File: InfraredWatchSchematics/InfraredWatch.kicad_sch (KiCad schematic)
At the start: 45 parts, among them J1 USB_C_Receptacle_USB2.0_14P, J2 Conn_Coaxial, J3 Micro_SD_Card_Det2, P1 XC9265A331MR-G, SW1 SW_Push, U1 STM32WB55CGU6, U2 MCP73831-5-OT, U3 USBLC6-2SC6, Y1 32MHz, Y2 32.768kHz

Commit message: Sat Mar 28 22:20:19 EDT 2026
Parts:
- removed J1: USB_C_Receptacle_USB2.0_14P, symbol Connector:USB_C_Receptacle_USB2.0_14P
- removed J2: Conn_Coaxial, symbol Connector:Conn_Coaxial
- added AE1: Antenna_Loop, symbol Device:Antenna_Loop
- added C20, C21, C22: 100nF, Capacitor_SMD:C_0402_1005Metric_Pad0.74x0.62mm_HandSolder, symbol Device:C
- added J4: USB_C_Receptacle_USB2.0_16P, Connector_USB:USB_C_Receptacle_G-Switch_GT-USB-7010ASV, symbol Connector:USB_C_Receptacle_USB2.0_16P
- added R10, R11, R12: 100, Resistor_SMD:R_0201_0603Metric_Pad0.64x0.40mm_HandSolder, symbol Device:R
- added R6, R7, R8: 5.1k, Resistor_SMD:R_0603_1608Metric_Pad0.98x0.95mm_HandSolder, symbol Device:R
- added SW1, SW2, SW3: SW_Push, symbol Switch:SW_Push
- C1: renamed from C17; footprint (none) -> Capacitor_SMD:C_0603_1608Metric_Pad1.08x0.95mm_HandSolder
- C10: renamed from C9; footprint (none) -> Capacitor_SMD:C_0603_1608Metric_Pad1.08x0.95mm_HandSolder
- C11: renamed from C19; footprint (none) -> Capacitor_SMD:C_0201_0603Metric_Pad0.64x0.40mm_HandSolder
- C12: renamed from C10; footprint (none) -> Capacitor_SMD:C_0402_1005Metric_Pad0.74x0.62mm_HandSolder
- C13: renamed from C8; footprint (none) -> Capacitor_SMD:C_0402_1005Metric_Pad0.74x0.62mm_HandSolder
- C14: renamed from C20; footprint (none) -> Capacitor_SMD:C_0402_1005Metric_Pad0.74x0.62mm_HandSolder
- C15: renamed from C12; footprint (none) -> Capacitor_SMD:C_0402_1005Metric_Pad0.74x0.62mm_HandSolder
- C16: renamed from C13; footprint (none) -> Capacitor_SMD:C_0402_1005Metric_Pad0.74x0.62mm_HandSolder
- C17: renamed from C11; footprint (none) -> Capacitor_SMD:C_0603_1608Metric_Pad1.08x0.95mm_HandSolder
- C18: renamed from C14; footprint (none) -> Capacitor_SMD:C_0402_1005Metric_Pad0.74x0.62mm_HandSolder
- C19: renamed from C15; footprint (none) -> Capacitor_SMD:C_0402_1005Metric_Pad0.74x0.62mm_HandSolder
- C2: renamed from C7; footprint (none) -> Capacitor_SMD:C_0603_1608Metric_Pad1.08x0.95mm_HandSolder
- C23: renamed from C16; footprint (none) -> Capacitor_SMD:C_0402_1005Metric_Pad0.74x0.62mm_HandSolder
- C3: renamed from C6; footprint (none) -> Capacitor_SMD:C_0402_1005Metric_Pad0.74x0.62mm_HandSolder
- C4: renamed from C5; footprint (none) -> Capacitor_SMD:C_0402_1005Metric_Pad0.74x0.62mm_HandSolder
- C5: renamed from C4; footprint (none) -> Capacitor_SMD:C_0402_1005Metric_Pad0.74x0.62mm_HandSolder
- C6: renamed from C18; footprint (none) -> Capacitor_SMD:C_0201_0603Metric_Pad0.64x0.40mm_HandSolder
- C7: renamed from C3; footprint (none) -> Capacitor_SMD:C_0402_1005Metric_Pad0.74x0.62mm_HandSolder
- C8: renamed from C2; footprint (none) -> Capacitor_SMD:C_0402_1005Metric_Pad0.74x0.62mm_HandSolder
- C9: renamed from C1; footprint (none) -> Capacitor_SMD:C_0402_1005Metric_Pad0.74x0.62mm_HandSolder
- D1: renamed from D2; footprint (none) -> LED_SMD:LED_0402_1005Metric_Pad0.77x0.64mm_HandSolder
- D2: renamed from D1; footprint (none) -> LED_SMD:LED_0402_1005Metric_Pad0.77x0.64mm_HandSolder
- L1: renamed from L4; footprint (none) -> Inductor_SMD:L_0603_1608Metric_Pad1.05x0.95mm_HandSolder
- L2: renamed from L1; footprint (none) -> Inductor_SMD:L_0603_1608Metric_Pad1.05x0.95mm_HandSolder
- L3: renamed from L2; footprint (none) -> Inductor_SMD:L_0603_1608Metric_Pad1.05x0.95mm_HandSolder
- L4: renamed from L3; footprint (none) -> Inductor_SMD:L_0603_1608Metric_Pad1.05x0.95mm_HandSolder
- R1: renamed from R7; footprint (none) -> Resistor_SMD:R_0603_1608Metric_Pad0.98x0.95mm_HandSolder
- R13: renamed from R4; footprint (none) -> Resistor_SMD:R_0201_0603Metric_Pad0.64x0.40mm_HandSolder
- R2: renamed from R6; footprint (none) -> Resistor_SMD:R_0201_0603Metric_Pad0.64x0.40mm_HandSolder
- R3: renamed from R1; footprint (none) -> Resistor_SMD:R_0603_1608Metric_Pad0.98x0.95mm_HandSolder
- R4: renamed from R2; footprint (none) -> Resistor_SMD:R_0603_1608Metric_Pad0.98x0.95mm_HandSolder
- R5: footprint (none) -> Resistor_SMD:R_0603_1608Metric_Pad0.98x0.95mm_HandSolder
- R9: renamed from R3; footprint (none) -> Resistor_SMD:R_0603_1608Metric_Pad0.98x0.95mm_HandSolder
- Y1: renamed from Y2; footprint (none) -> Crystal:Crystal_SMD_2012-2Pin_2.0x1.2mm_HandSoldering
- Y2: renamed from Y1; footprint (none) -> Crystal:Crystal_SMD_SeikoEpson_FA128-4Pin_2.0x1.6mm
- renumbered J3 to J2, SW1 to SW4, U2 to U1, U3 to U2, U1 to U3
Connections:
- net +3.3V: now also SW1.2, SW2.2, SW3.2
- net CHARGE_IN: now also J4.A4 (VBUS), J4.A9 (VBUS), J4.B4 (VBUS), J4.B9 (VBUS)
- net GND: now also AE1.2, C20.2, C21.2, C22.2, J4.A1 (GND), J4.A12 (GND), J4.B1 (GND), J4.B12 (GND), J4.SH (SHIELD), R6.2, R7.2, R8.2
- net Button1: now reaches U3.10 (PA1)
- net Button1: now also C21.1, R11.1, R7.1
- net Button2: now reaches U3.11 (PA2)
- net Button2: now also C22.1, R12.1, R8.1
- net Button0: now reaches U3.9 (PA0)
- net Button0: now also C20.1, R10.1, R6.1
- net at FLT1.3 (OUT): now also AE1.1
- net at R3.1: now also J4.A5 (CC1)
- net at U2.1 (I/O1): now also J4.A7 (D-), J4.B7 (D-)
- net at U2.3 (I/O2): now also J4.A6 (D+), J4.B6 (D+)
- net at R4.1: now also J4.B5 (CC2)
- net BOOT0 renamed BOOT0/Button3
- new net: R12.2, SW3.1
- new net: R11.2, SW2.1
- new net: R10.2, SW1.1
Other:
- note added: "Button0-2"
- note added: "Button3/Boot"
- note removed: "P4 where?"
- company: (none) -> Alex Moore
- title: (none) -> ISP_Watch
- moved on the sheet: C10, C12, C13, C23, R13, R9, SW4, Y2

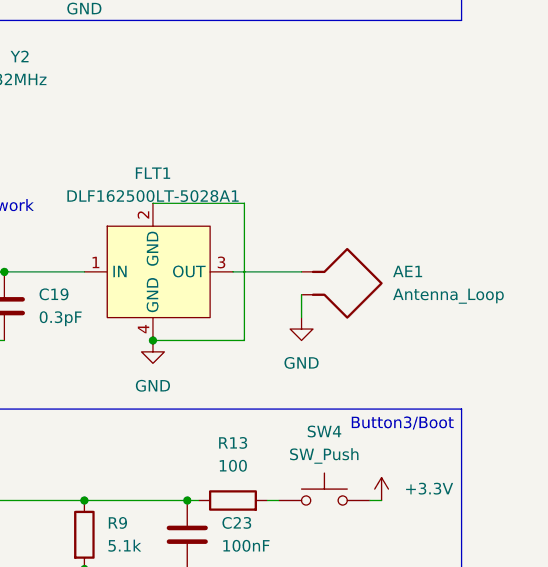
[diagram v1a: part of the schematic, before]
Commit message: Sun Mar 29 09:52:52 EDT 2026 added SMD ble chip
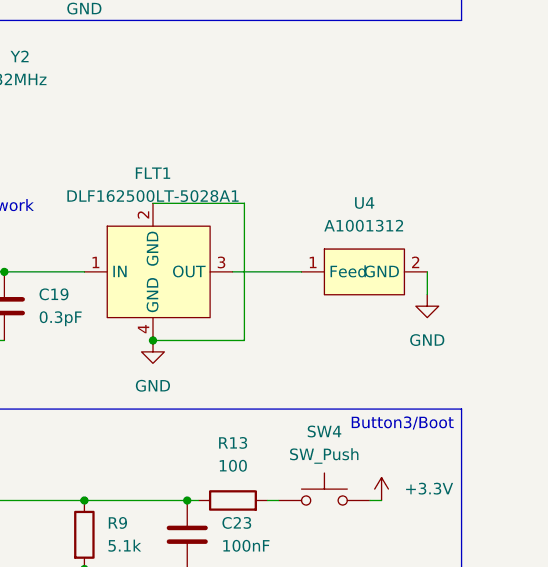
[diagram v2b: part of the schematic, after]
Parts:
- removed AE1: Antenna_Loop, symbol Device:Antenna_Loop
- added U4: A1001312, InfraredWatch:A1001312, symbol InfraredWatch:A1001312
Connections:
- net GND: now also U4.2 (GND)
- net at FLT1.3 (OUT): now also U4.1 (Feed)
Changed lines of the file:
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@@
 	(wire
 		(pts
-			(xy 266.7 93.98) (xy 266.7 96.52)
+			(xy 280.67 91.44) (xy 280.67 93.98)
 		)
 		(stroke
@@
 	)
 	(symbol
+		(lib_id "InfraredWatch:A1001312")
+		(at 273.05 91.44 0)
+		(unit 1)
+		(body_style 1)
+		(exclude_from_sim no)
+		(in_bom yes)
+		(on_board yes)
+		(in_pos_files yes)
+		(dnp no)
+		(fields_autoplaced yes)
+		(property "Reference" "U4"
+			(at 273.685 83.82 0)
+			(show_name no)
+			(do_not_autoplace no)
+			(effects
+				(font
+					(size 1.27 1.27)
+				)
+			)
+		)
+		(property "Value" "A1001312"
+			(at 273.685 86.36 0)
+			(show_name no)
+			(do_not_autoplace no)
+			(effects
+				(font
+					(size 1.27 1.27)
+				)
+			)
+		)
+		(property "Footprint" "InfraredWatch:A1001312"
+			(at 273.05 91.44 0)
+			(hide yes)
+			(show_name no)
+			(do_not_autoplace no)
+			(effects
+				(font
+					(size 1.27 1.27)
+				)
+			)
+		)
+		(property "Datasheet" "https://datasheets.kyocera-avx.com/A1001312.pdf"
+			(at 273.05 91.44 0)
+			(hide yes)
+			(show_name no)
+			(do_not_autoplace no)
+			(effects
+				(font
+					(size 1.27 1.27)
+				)
+			)
+		)
+		(property "Description" ""
+			(at 273.05 91.44 0)
+			(hide yes)
+			(show_name no)
+			(do_not_autoplace no)
+			(effects
+				(font
+					(size 1.27 1.27)
+				)
+			)
+		)
+		(pin "1"
+		)
+		(pin "2"
+		)
+		(instances
+			(project "InfraredWatch"
+				(path "/cfbb9194-e408-4c25-81c1-90611b33486f"
+					(reference "U4")
+					(unit 1)
+				)
+			)
+		)
+	)
+	(symbol
 		(lib_id "power:GND")
 		(at 242.57 43.18 0)
@@
 	(symbol
 		(lib_id "power:GND")
-		(at 266.7 96.52 0)
+		(at 280.67 93.98 0)
 		(unit 1)
 		(body_style 1)
@@
 		(fields_autoplaced yes)
 		(property "Reference" "#PWR031"
-			(at 266.7 102.87 0)
+			(at 280.67 100.33 0)
 			(hide yes)
 			(show_name no)
@@
 		)
 		(property "Value" "GND"
-			(at 266.7 101.6 0)
+			(at 280.67 99.06 0)
 			(show_name no)
 			(do_not_autoplace no)
@@
 		)
 		(property "Footprint" ""
-			(at 266.7 96.52 0)
+			(at 280.67 93.98 0)
 			(hide yes)
 			(show_name no)
@@
 		)
 		(property "Datasheet" ""
-			(at 266.7 96.52 0)
+			(at 280.67 93.98 0)
 			(hide yes)
 			(show_name no)
@@
 		)
 		(property "Description" "Power symbol creates a global label with name \"GND\" , ground"
-			(at 266.7 96.52 0)
+			(at 280.67 93.98 0)
 			(hide yes)
 			(show_name no)
@@
 					(unit 1)
 				)
-			)
-		)
-	)
-	(symbol
-		(lib_id "Device:Antenna_Loop")
-		(at 271.78 91.44 270)
-		(unit 1)
-		(body_style 1)
-		(exclude_from_sim no)
-		(in_bom yes)
-		(on_board yes)
-		(in_pos_files yes)
-		(dnp no)
-		(fields_autoplaced yes)
-		(property "Reference" "AE1"
-			(at 276.86 91.44 90)
-			(show_name no)
-			(do_not_autoplace no)
-			(effects
-				(font
-					(size 1.27 1.27)
-				)
-				(justify left)
-			)
-		)
-		(property "Value" "Antenna_Loop"
-			(at 276.86 93.98 90)
-			(show_name no)
-			(do_not_autoplace no)
-			(effects
-				(font
-					(size 1.27 1.27)
-				)
-				(justify left)
-			)
-		)
-		(property "Footprint" ""
-			(at 271.78 91.44 0)
-			(hide yes)
-			(show_name no)
-			(do_not_autoplace no)
-			(effects
-				(font
-					(size 1.27 1.27)
-				)
-			)
-		)
-		(property "Datasheet" ""
-			(at 271.78 91.44 0)
-			(hide yes)
-			(show_name no)
-			(do_not_autoplace no)
-			(effects
-				(font
-					(size 1.27 1.27)
-				)
-			)
-		)
-		(property "Description" "Loop antenna"
-			(at 271.78 91.44 0)
-			(hide yes)
-			(show_name no)
-			(do_not_autoplace no)
-			(effects
-				(font
-					(size 1.27 1.27)
-				)
-			)
-		)
-		(pin "1"
-		)
-		(pin "2"
-		)
-		(instances
-			(project "InfraredWatch"
-				(path "/cfbb9194-e408-4c25-81c1-90611b33486f"
-					(reference "AE1")
-					(unit 1)
-				)

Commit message: Thu Apr  2 09:39:45 EDT 2026 | updated pcb
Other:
- added sheet NFC (nfc.kicad_sch)
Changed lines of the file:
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@@
+		)
+	)
+	(sheet
+		(at 96.52 134.62)
+		(size 22.86 24.13)
+		(exclude_from_sim no)
+		(in_bom yes)
+		(on_board yes)
+		(dnp no)
+		(fields_autoplaced yes)
+		(stroke
+			(width 0.1524)
+			(type solid)
+		)
+		(fill
+			(color 0 0 0 0)
+		)
+		(property "Sheetname" "NFC"
+			(at 96.52 133.9084 0)
+			(show_name yes)
+			(do_not_autoplace no)
+			(effects
+				(font
+					(size 1.27 1.27)
+				)
+				(justify left bottom)
+			)
+		)
+		(property "Sheetfile" "nfc.kicad_sch"
+			(at 96.52 159.3346 0)
+			(show_name yes)
+			(do_not_autoplace no)
+			(effects
+				(font
+					(size 1.27 1.27)
+				)
+				(justify left top)
+			)
+		)
+		(instances
+			(project "InfraredWatch"
+				(path "/cfbb9194-e408-4c25-81c1-90611b33486f"
+					(page "2")
+				)
+			)
 		)
 	)

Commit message: Wed Apr 29 09:42:28 EDT 2026 | updated pcb
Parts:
- C6: footprint Capacitor_SMD:C_0201_0603Metric_Pad0.64x0.40mm_HandSolder -> Capacitor_SMD:C_0603_1608Metric_Pad1.08x0.95mm_HandSolder
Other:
- removed sheet NFC
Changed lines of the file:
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@@
 		(title "ISP_Watch")
 		(date "2026-03-28")
-		(rev "0")
+		(rev "0.0")
 		(company "Alex Moore")
 	)
@@
 			)
 		)
-		(property "Footprint" "Capacitor_SMD:C_0201_0603Metric_Pad0.64x0.40mm_HandSolder"
+		(property "Footprint" "Capacitor_SMD:C_0603_1608Metric_Pad1.08x0.95mm_HandSolder"
 			(at 58.1152 153.67 0)
 			(hide yes)
@@
 				)
 			)
-		)
-	)
-	(sheet
-		(at 96.52 134.62)
-		(size 22.86 24.13)
-		(exclude_from_sim no)
-		(in_bom yes)
-		(on_board yes)
-		(dnp no)
-		(fields_autoplaced yes)
-		(stroke
-			(width 0.1524)
-			(type solid)
-		)
-		(fill
-			(color 0 0 0 0)
-		)
-		(property "Sheetname" "NFC"
-			(at 96.52 133.9084 0)
-			(show_name yes)
-			(do_not_autoplace no)
-			(effects
-				(font
-					(size 1.27 1.27)
-				)
-				(justify left bottom)
-			)
-		)
-		(property "Sheetfile" "nfc.kicad_sch"
-			(at 96.52 159.3346 0)
-			(show_name yes)
-			(do_not_autoplace no)
-			(effects
-				(font
-					(size 1.27 1.27)
-				)
-				(justify left top)
-			)
-		)
-		(instances
-			(project "InfraredWatch"
-				(path "/cfbb9194-e408-4c25-81c1-90611b33486f"
-					(page "2")
-				)
-			)
